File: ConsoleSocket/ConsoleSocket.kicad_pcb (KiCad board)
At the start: 2 copper layers, 112.9 x 12.7 mm, 4 parts, among them J1 Conn_01x05_Male, J3 Conn_02x25_Odd_Even

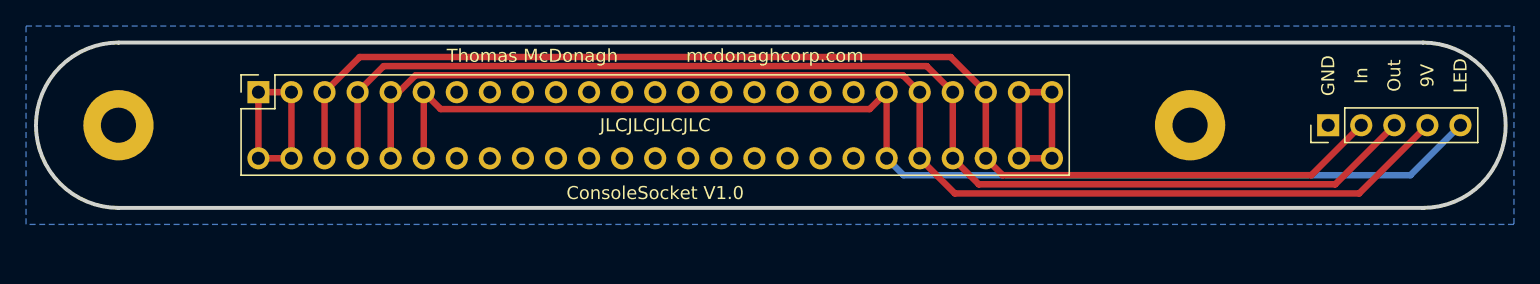
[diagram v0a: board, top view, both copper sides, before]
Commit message: Fixed socket to fit screws and space easier
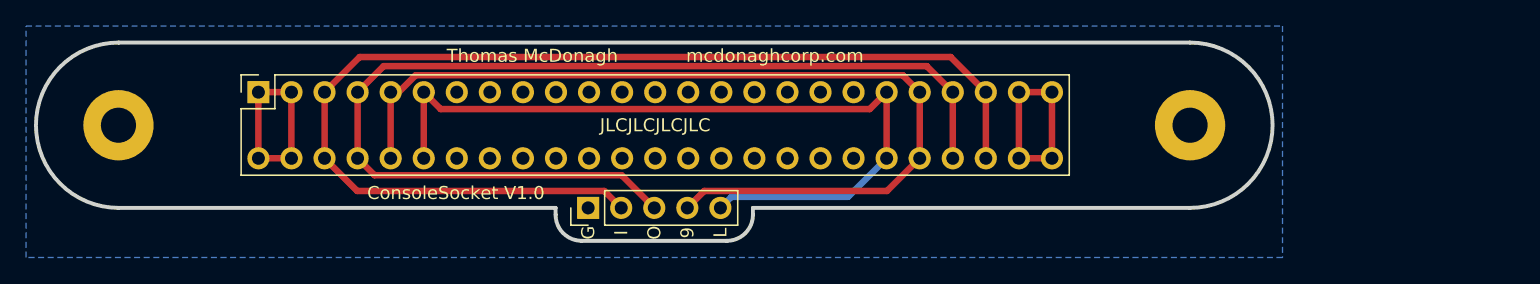
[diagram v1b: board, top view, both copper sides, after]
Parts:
- moved J1 57.2 mm to (132.1, 45.7)
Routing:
- net /LEDPower: track 93.6 -> 61.8 mm
- net +9V: track 94.8 -> 71.9 mm
- net /Output: track 94.2 -> 81.9 mm
- net /Input: track 94.8 -> 88.2 mm
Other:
- board size 112.9 x 12.7 mm -> 95 x 15.2 mm
- board text added: "9"
- board text added: "G"
- board text added: "I"
- board text added: "L"
- board text added: "O"
- board text removed: "9V"
- board text removed: "GND"
- board text removed: "In"
- board text removed: "LED"
- board text removed: "Out"

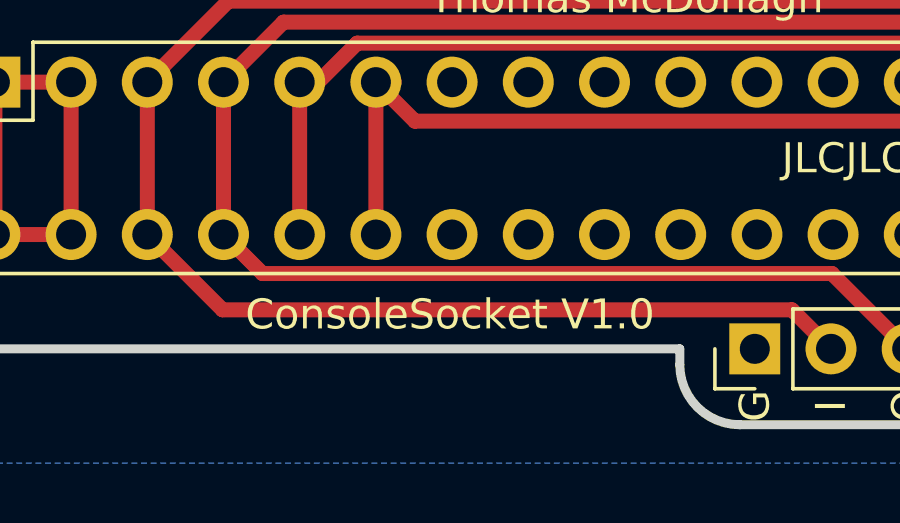
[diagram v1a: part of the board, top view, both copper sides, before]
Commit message: Fixed silkscreen
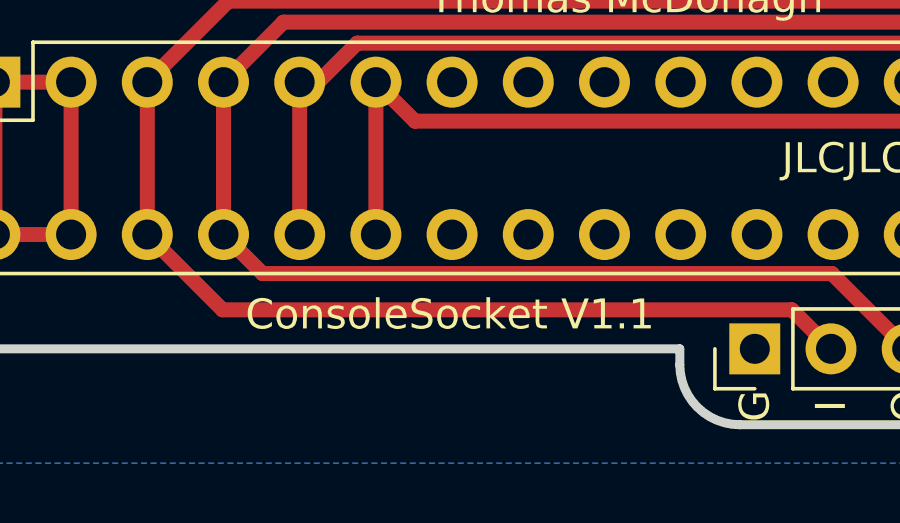
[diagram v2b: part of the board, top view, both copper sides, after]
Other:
- board text added: "ConsoleSocket V1.1"
- board text removed: "ConsoleSocket V1.0"
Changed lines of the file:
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@@
   )
   (setup
-    (last_trace_width 0.5)
+    (last_trace_width 0.25)
     (user_trace_width 0.5)
     (trace_clearance 0.2)
@@
       (effects (font (size 1 1) (thickness 0.15)))
     )
+    (fp_line (start -6.88 62.7) (end -6.88 -1.8) (layer F.CrtYd) (width 0.05))
+    (fp_line (start 1.76 62.7) (end -6.88 62.7) (layer F.CrtYd) (width 0.05))
+    (fp_line (start 1.76 -1.8) (end 1.76 62.7) (layer F.CrtYd) (width 0.05))
+    (fp_line (start -6.88 -1.8) (end 1.76 -1.8) (layer F.CrtYd) (width 0.05))
+    (fp_line (start 0 -1.33) (end 1.33 -1.33) (layer F.SilkS) (width 0.12))
+    (fp_line (start 1.33 -1.33) (end 1.33 0) (layer F.SilkS) (width 0.12))
+    (fp_line (start -1.27 -1.33) (end -1.27 1.27) (layer F.SilkS) (width 0.12))
+    (fp_line (start -1.27 1.27) (end 1.33 1.27) (layer F.SilkS) (width 0.12))
+    (fp_line (start 1.33 1.27) (end 1.33 62.29) (layer F.SilkS) (width 0.12))
+    (fp_line (start -6.38 62.29) (end 1.33 62.29) (layer F.SilkS) (width 0.12))
+    (fp_line (start -6.38 -1.33) (end -6.38 62.29) (layer F.SilkS) (width 0.12))
+    (fp_line (start -6.38 -1.33) (end -1.27 -1.33) (layer F.SilkS) (width 0.12))
+    (fp_line (start -6.35 62.23) (end -6.35 -1.27) (layer F.Fab) (width 0.1))
+    (fp_line (start 1.27 62.23) (end -6.35 62.23) (layer F.Fab) (width 0.1))
+    (fp_line (start 1.27 -0.27) (end 1.27 62.23) (layer F.Fab) (width 0.1))
+    (fp_line (start 0.27 -1.27) (end 1.27 -0.27) (layer F.Fab) (width 0.1))
     (fp_line (start -6.35 -1.27) (end 0.27 -1.27) (layer F.Fab) (width 0.1))
-    (fp_line (start 0.27 -1.27) (end 1.27 -0.27) (layer F.Fab) (width 0.1))
-    (fp_line (start 1.27 -0.27) (end 1.27 62.23) (layer F.Fab) (width 0.1))
-    (fp_line (start 1.27 62.23) (end -6.35 62.23) (layer F.Fab) (width 0.1))
-    (fp_line (start -6.35 62.23) (end -6.35 -1.27) (layer F.Fab) (width 0.1))
-    (fp_line (start -6.38 -1.33) (end -1.27 -1.33) (layer F.SilkS) (width 0.12))
-    (fp_line (start -6.38 -1.33) (end -6.38 62.29) (layer F.SilkS) (width 0.12))
-    (fp_line (start -6.38 62.29) (end 1.33 62.29) (layer F.SilkS) (width 0.12))
-    (fp_line (start 1.33 1.27) (end 1.33 62.29) (layer F.SilkS) (width 0.12))
-    (fp_line (start -1.27 1.27) (end 1.33 1.27) (layer F.SilkS) (width 0.12))
-    (fp_line (start -1.27 -1.33) (end -1.27 1.27) (layer F.SilkS) (width 0.12))
-    (fp_line (start 1.33 -1.33) (end 1.33 0) (layer F.SilkS) (width 0.12))
-    (fp_line (start 0 -1.33) (end 1.33 -1.33) (layer F.SilkS) (width 0.12))
-    (fp_line (start -6.88 -1.8) (end 1.76 -1.8) (layer F.CrtYd) (width 0.05))
-    (fp_line (start 1.76 -1.8) (end 1.76 62.7) (layer F.CrtYd) (width 0.05))
-    (fp_line (start 1.76 62.7) (end -6.88 62.7) (layer F.CrtYd) (width 0.05))
-    (fp_line (start -6.88 62.7) (end -6.88 -1.8) (layer F.CrtYd) (width 0.05))
     (fp_text user %R (at -1.27 30.48 180) (layer F.Fab)
       (effects (font (size 1 1) (thickness 0.15)))
@@
       (effects (font (size 1 1) (thickness 0.15)))
     )
+    (fp_line (start 1.8 -1.8) (end -1.8 -1.8) (layer F.CrtYd) (width 0.05))
+    (fp_line (start 1.8 11.95) (end 1.8 -1.8) (layer F.CrtYd) (width 0.05))
+    (fp_line (start -1.8 11.95) (end 1.8 11.95) (layer F.CrtYd) (width 0.05))
+    (fp_line (start -1.8 -1.8) (end -1.8 11.95) (layer F.CrtYd) (width 0.05))
+    (fp_line (start -1.33 -1.33) (end 0 -1.33) (layer F.SilkS) (width 0.12))
+    (fp_line (start -1.33 0) (end -1.33 -1.33) (layer F.SilkS) (width 0.12))
+    (fp_line (start -1.33 1.27) (end 1.33 1.27) (layer F.SilkS) (width 0.12))
+    (fp_line (start 1.33 1.27) (end 1.33 11.49) (layer F.SilkS) (width 0.12))
+    (fp_line (start -1.33 1.27) (end -1.33 11.49) (layer F.SilkS) (width 0.12))
+    (fp_line (start -1.33 11.49) (end 1.33 11.49) (layer F.SilkS) (width 0.12))
+    (fp_line (start -1.27 -0.635) (end -0.635 -1.27) (layer F.Fab) (width 0.1))
+    (fp_line (start -1.27 11.43) (end -1.27 -0.635) (layer F.Fab) (width 0.1))
+    (fp_line (start 1.27 11.43) (end -1.27 11.43) (layer F.Fab) (width 0.1))
+    (fp_line (start 1.27 -1.27) (end 1.27 11.43) (layer F.Fab) (width 0.1))
     (fp_line (start -0.635 -1.27) (end 1.27 -1.27) (layer F.Fab) (width 0.1))
-    (fp_line (start 1.27 -1.27) (end 1.27 11.43) (layer F.Fab) (width 0.1))
-    (fp_line (start 1.27 11.43) (end -1.27 11.43) (layer F.Fab) (width 0.1))
-    (fp_line (start -1.27 11.43) (end -1.27 -0.635) (layer F.Fab) (width 0.1))
-    (fp_line (start -1.27 -0.635) (end -0.635 -1.27) (layer F.Fab) (width 0.1))
-    (fp_line (start -1.33 11.49) (end 1.33 11.49) (layer F.SilkS) (width 0.12))
-    (fp_line (start -1.33 1.27) (end -1.33 11.49) (layer F.SilkS) (width 0.12))
-    (fp_line (start 1.33 1.27) (end 1.33 11.49) (layer F.SilkS) (width 0.12))
-    (fp_line (start -1.33 1.27) (end 1.33 1.27) (layer F.SilkS) (width 0.12))
-    (fp_line (start -1.33 0) (end -1.33 -1.33) (layer F.SilkS) (width 0.12))
-    (fp_line (start -1.33 -1.33) (end 0 -1.33) (layer F.SilkS) (width 0.12))
-    (fp_line (start -1.8 -1.8) (end -1.8 11.95) (layer F.CrtYd) (width 0.05))
-    (fp_line (start -1.8 11.95) (end 1.8 11.95) (layer F.CrtYd) (width 0.05))
-    (fp_line (start 1.8 11.95) (end 1.8 -1.8) (layer F.CrtYd) (width 0.05))
-    (fp_line (start 1.8 -1.8) (end -1.8 -1.8) (layer F.CrtYd) (width 0.05))
     (fp_text user %R (at 0 5.08) (layer F.Fab)
       (effects (font (size 1 1) (thickness 0.15)))
@@
       (effects (font (size 1 1) (thickness 0.15)))
     )
+    (fp_circle (center 0 0) (end 2.95 0) (layer F.CrtYd) (width 0.05))
     (fp_circle (center 0 0) (end 2.7 0) (layer Cmts.User) (width 0.15))
-    (fp_circle (center 0 0) (end 2.95 0) (layer F.CrtYd) (width 0.05))
     (fp_text user %R (at 0.3 0) (layer F.Fab)
       (effects (font (size 1 1) (thickness 0.15)))
@@
       (effects (font (size 1 1) (thickness 0.15)))
     )
+    (fp_circle (center 0 0) (end 2.7 0) (layer Cmts.User) (width 0.15))
     (fp_circle (center 0 0) (end 2.95 0) (layer F.CrtYd) (width 0.05))
-    (fp_circle (center 0 0) (end 2.7 0) (layer Cmts.User) (width 0.15))
     (fp_text user %R (at 0.3 0) (layer F.Fab)
       (effects (font (size 1 1) (thickness 0.15)))
@@
     (effects (font (size 1 1) (thickness 0.15)) (justify mirror))
   )
-  (gr_text "ConsoleSocket V1.0" (at 121.92 44.577) (layer B.SilkS)
+  (gr_text "ConsoleSocket V1.1" (at 121.92 44.577) (layer B.SilkS)
     (effects (font (size 1 1) (thickness 0.15)) (justify mirror))
   )
-  (gr_text "ConsoleSocket V1.0" (at 121.92 44.577) (layer F.SilkS)
-    (effects (font (size 1 1) (thickness 0.15)))
-  )
+  (gr_text "ConsoleSocket V1.1" (at 121.92 44.577) (layer F.SilkS)
+    (effects (font (size 1 1) (thickness 0.15)))
+  )

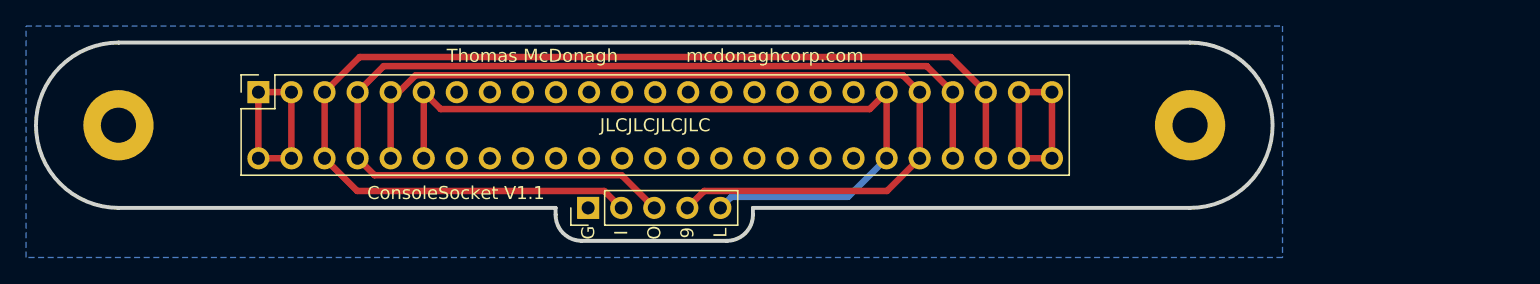
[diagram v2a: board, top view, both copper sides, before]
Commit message: Fixed silkscreen
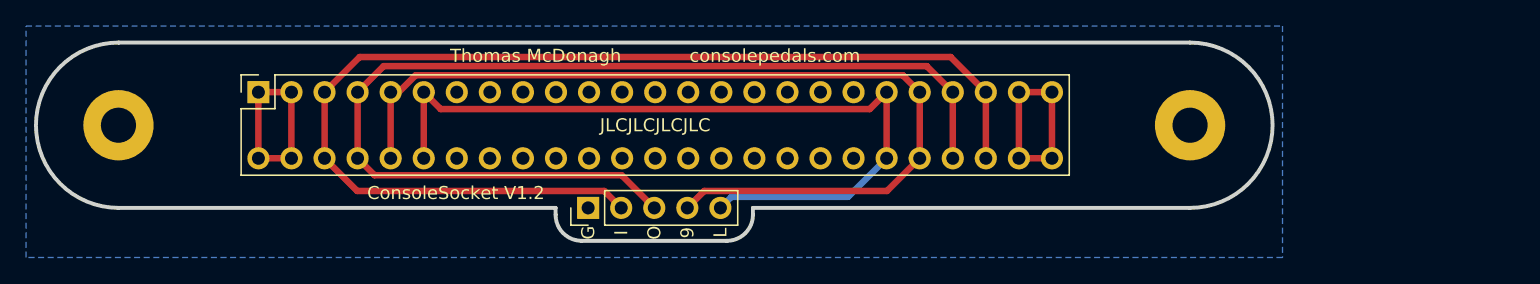
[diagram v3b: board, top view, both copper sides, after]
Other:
- board text added: "ConsoleSocket V1.2"
- board text added: "Thomas McDonagh consolepedals.com"
- board text removed: "ConsoleSocket V1.1"
- board text removed: "Thomas McDonagh mcdonaghcorp.com"
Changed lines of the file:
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@@
   (general
     (thickness 1.6)
-    (drawings 20)
+    (drawings 25)
     (tracks 44)
     (zones 0)
@@
       (effects (font (size 1 1) (thickness 0.15)))
     )
+    (fp_line (start -6.35 -1.27) (end 0.27 -1.27) (layer F.Fab) (width 0.1))
+    (fp_line (start 0.27 -1.27) (end 1.27 -0.27) (layer F.Fab) (width 0.1))
+    (fp_line (start 1.27 -0.27) (end 1.27 62.23) (layer F.Fab) (width 0.1))
+    (fp_line (start 1.27 62.23) (end -6.35 62.23) (layer F.Fab) (width 0.1))
+    (fp_line (start -6.35 62.23) (end -6.35 -1.27) (layer F.Fab) (width 0.1))
+    (fp_line (start -6.38 -1.33) (end -1.27 -1.33) (layer F.SilkS) (width 0.12))
+    (fp_line (start -6.38 -1.33) (end -6.38 62.29) (layer F.SilkS) (width 0.12))
+    (fp_line (start -6.38 62.29) (end 1.33 62.29) (layer F.SilkS) (width 0.12))
+    (fp_line (start 1.33 1.27) (end 1.33 62.29) (layer F.SilkS) (width 0.12))
+    (fp_line (start -1.27 1.27) (end 1.33 1.27) (layer F.SilkS) (width 0.12))
+    (fp_line (start -1.27 -1.33) (end -1.27 1.27) (layer F.SilkS) (width 0.12))
+    (fp_line (start 1.33 -1.33) (end 1.33 0) (layer F.SilkS) (width 0.12))
+    (fp_line (start 0 -1.33) (end 1.33 -1.33) (layer F.SilkS) (width 0.12))
+    (fp_line (start -6.88 -1.8) (end 1.76 -1.8) (layer F.CrtYd) (width 0.05))
+    (fp_line (start 1.76 -1.8) (end 1.76 62.7) (layer F.CrtYd) (width 0.05))
+    (fp_line (start 1.76 62.7) (end -6.88 62.7) (layer F.CrtYd) (width 0.05))
     (fp_line (start -6.88 62.7) (end -6.88 -1.8) (layer F.CrtYd) (width 0.05))
-    (fp_line (start 1.76 62.7) (end -6.88 62.7) (layer F.CrtYd) (width 0.05))
-    (fp_line (start 1.76 -1.8) (end 1.76 62.7) (layer F.CrtYd) (width 0.05))
-    (fp_line (start -6.88 -1.8) (end 1.76 -1.8) (layer F.CrtYd) (width 0.05))
-    (fp_line (start 0 -1.33) (end 1.33 -1.33) (layer F.SilkS) (width 0.12))
-    (fp_line (start 1.33 -1.33) (end 1.33 0) (layer F.SilkS) (width 0.12))
-    (fp_line (start -1.27 -1.33) (end -1.27 1.27) (layer F.SilkS) (width 0.12))
-    (fp_line (start -1.27 1.27) (end 1.33 1.27) (layer F.SilkS) (width 0.12))
-    (fp_line (start 1.33 1.27) (end 1.33 62.29) (layer F.SilkS) (width 0.12))
-    (fp_line (start -6.38 62.29) (end 1.33 62.29) (layer F.SilkS) (width 0.12))
-    (fp_line (start -6.38 -1.33) (end -6.38 62.29) (layer F.SilkS) (width 0.12))
-    (fp_line (start -6.38 -1.33) (end -1.27 -1.33) (layer F.SilkS) (width 0.12))
-    (fp_line (start -6.35 62.23) (end -6.35 -1.27) (layer F.Fab) (width 0.1))
-    (fp_line (start 1.27 62.23) (end -6.35 62.23) (layer F.Fab) (width 0.1))
-    (fp_line (start 1.27 -0.27) (end 1.27 62.23) (layer F.Fab) (width 0.1))
-    (fp_line (start 0.27 -1.27) (end 1.27 -0.27) (layer F.Fab) (width 0.1))
-    (fp_line (start -6.35 -1.27) (end 0.27 -1.27) (layer F.Fab) (width 0.1))
     (fp_text user %R (at -1.27 30.48 180) (layer F.Fab)
       (effects (font (size 1 1) (thickness 0.15)))
@@
       (effects (font (size 1 1) (thickness 0.15)))
     )
+    (fp_line (start -0.635 -1.27) (end 1.27 -1.27) (layer F.Fab) (width 0.1))
+    (fp_line (start 1.27 -1.27) (end 1.27 11.43) (layer F.Fab) (width 0.1))
+    (fp_line (start 1.27 11.43) (end -1.27 11.43) (layer F.Fab) (width 0.1))
+    (fp_line (start -1.27 11.43) (end -1.27 -0.635) (layer F.Fab) (width 0.1))
+    (fp_line (start -1.27 -0.635) (end -0.635 -1.27) (layer F.Fab) (width 0.1))
+    (fp_line (start -1.33 11.49) (end 1.33 11.49) (layer F.SilkS) (width 0.12))
+    (fp_line (start -1.33 1.27) (end -1.33 11.49) (layer F.SilkS) (width 0.12))
+    (fp_line (start 1.33 1.27) (end 1.33 11.49) (layer F.SilkS) (width 0.12))
+    (fp_line (start -1.33 1.27) (end 1.33 1.27) (layer F.SilkS) (width 0.12))
+    (fp_line (start -1.33 0) (end -1.33 -1.33) (layer F.SilkS) (width 0.12))
+    (fp_line (start -1.33 -1.33) (end 0 -1.33) (layer F.SilkS) (width 0.12))
+    (fp_line (start -1.8 -1.8) (end -1.8 11.95) (layer F.CrtYd) (width 0.05))
+    (fp_line (start -1.8 11.95) (end 1.8 11.95) (layer F.CrtYd) (width 0.05))
+    (fp_line (start 1.8 11.95) (end 1.8 -1.8) (layer F.CrtYd) (width 0.05))
     (fp_line (start 1.8 -1.8) (end -1.8 -1.8) (layer F.CrtYd) (width 0.05))
-    (fp_line (start 1.8 11.95) (end 1.8 -1.8) (layer F.CrtYd) (width 0.05))
-    (fp_line (start -1.8 11.95) (end 1.8 11.95) (layer F.CrtYd) (width 0.05))
-    (fp_line (start -1.8 -1.8) (end -1.8 11.95) (layer F.CrtYd) (width 0.05))
-    (fp_line (start -1.33 -1.33) (end 0 -1.33) (layer F.SilkS) (width 0.12))
-    (fp_line (start -1.33 0) (end -1.33 -1.33) (layer F.SilkS) (width 0.12))
-    (fp_line (start -1.33 1.27) (end 1.33 1.27) (layer F.SilkS) (width 0.12))
-    (fp_line (start 1.33 1.27) (end 1.33 11.49) (layer F.SilkS) (width 0.12))
-    (fp_line (start -1.33 1.27) (end -1.33 11.49) (layer F.SilkS) (width 0.12))
-    (fp_line (start -1.33 11.49) (end 1.33 11.49) (layer F.SilkS) (width 0.12))
-    (fp_line (start -1.27 -0.635) (end -0.635 -1.27) (layer F.Fab) (width 0.1))
-    (fp_line (start -1.27 11.43) (end -1.27 -0.635) (layer F.Fab) (width 0.1))
-    (fp_line (start 1.27 11.43) (end -1.27 11.43) (layer F.Fab) (width 0.1))
-    (fp_line (start 1.27 -1.27) (end 1.27 11.43) (layer F.Fab) (width 0.1))
-    (fp_line (start -0.635 -1.27) (end 1.27 -1.27) (layer F.Fab) (width 0.1))
     (fp_text user %R (at 0 5.08) (layer F.Fab)
       (effects (font (size 1 1) (thickness 0.15)))
@@
       (effects (font (size 1 1) (thickness 0.15)))
     )
+    (fp_circle (center 0 0) (end 2.7 0) (layer Cmts.User) (width 0.15))
     (fp_circle (center 0 0) (end 2.95 0) (layer F.CrtYd) (width 0.05))
-    (fp_circle (center 0 0) (end 2.7 0) (layer Cmts.User) (width 0.15))
     (fp_text user %R (at 0.3 0) (layer F.Fab)
       (effects (font (size 1 1) (thickness 0.15)))
@@
       (effects (font (size 1 1) (thickness 0.15)))
     )
+    (fp_circle (center 0 0) (end 2.95 0) (layer F.CrtYd) (width 0.05))
     (fp_circle (center 0 0) (end 2.7 0) (layer Cmts.User) (width 0.15))
-    (fp_circle (center 0 0) (end 2.95 0) (layer F.CrtYd) (width 0.05))
     (fp_text user %R (at 0.3 0) (layer F.Fab)
       (effects (font (size 1 1) (thickness 0.15)))
@@
     (pad 1 thru_hole circle (at 0 0) (size 5.4 5.4) (drill 2.7) (layers *.Cu *.Mask)
       (net 3 GND))
+  )
+  (gr_text "L\n" (at 142.24 47.625 90) (layer F.SilkS)
+    (effects (font (size 1 1) (thickness 0.15)))
+  )
+  (gr_text 9 (at 139.7 47.625 90) (layer F.SilkS)
+    (effects (font (size 1 1) (thickness 0.15)))
+  )
+  (gr_text O (at 137.16 47.625 90) (layer F.SilkS)
+    (effects (font (size 1 1) (thickness 0.15)))
+  )
+  (gr_text I (at 134.62 47.625 90) (layer F.SilkS)
+    (effects (font (size 1 1) (thickness 0.15)))
+  )
+  (gr_text G (at 132.08 47.625 90) (layer F.SilkS)
+    (effects (font (size 1 1) (thickness 0.15)))
   )
   (gr_line (start 144.74 45.72) (end 144.74 46.25) (layer Edge.Cuts) (width 0.3))
@@
   (gr_arc (start 131.58 46.25) (end 129.58 46.25) (angle -90) (layer Edge.Cuts) (width 0.3))
   (gr_arc (start 142.74 46.25) (end 142.74 48.25) (angle -90) (layer Edge.Cuts) (width 0.3))
-  (gr_text "L\n" (at 142.24 47.625 90) (layer F.SilkS)
-    (effects (font (size 1 1) (thickness 0.15)))
-  )
-  (gr_text 9 (at 139.7 47.625 90) (layer F.SilkS)
-    (effects (font (size 1 1) (thickness 0.15)))
-  )
-  (gr_text O (at 137.16 47.625 90) (layer F.SilkS)
-    (effects (font (size 1 1) (thickness 0.15)))
-  )
-  (gr_text I (at 134.62 47.625 90) (layer F.SilkS)
-    (effects (font (size 1 1) (thickness 0.15)))
-  )
-  (gr_text G (at 132.08 47.625 90) (layer F.SilkS)
-    (effects (font (size 1 1) (thickness 0.15)))
-  )
-  (gr_text "Thomas McDonagh            mcdonaghcorp.com" (at 137.23 34.036) (layer B.SilkS)
-    (effects (font (size 1 1) (thickness 0.15)) (justify mirror))
-  )
-  (gr_text "ConsoleSocket V1.1" (at 121.92 44.577) (layer B.SilkS)
-    (effects (font (size 1 1) (thickness 0.15)) (justify mirror))
-  )
-  (gr_text "ConsoleSocket V1.1" (at 121.92 44.577) (layer F.SilkS)
-    (effects (font (size 1 1) (thickness 0.15)))
-  )
-  (gr_text "Thomas McDonagh            mcdonaghcorp.com" (at 137.23 34.036) (layer F.SilkS)
-    (effects (font (size 1 1) (thickness 0.15)))
-  )
+  (gr_text "L\n" (at 142.24 47.625 90) (layer B.SilkS)
+    (effects (font (size 1 1) (thickness 0.15)) (justify mirror))
+  )
+  (gr_text 9 (at 139.7 47.625 90) (layer B.SilkS)
+    (effects (font (size 1 1) (thickness 0.15)) (justify mirror))
+  )
+  (gr_text O (at 137.16 47.625 90) (layer B.SilkS)
+    (effects (font (size 1 1) (thickness 0.15)) (justify mirror))
+  )
+  (gr_text I (at 134.62 47.625 90) (layer B.SilkS)
+    (effects (font (size 1 1) (thickness 0.15)) (justify mirror))
+  )
+  (gr_text G (at 132.08 47.625 90) (layer B.SilkS)
+    (effects (font (size 1 1) (thickness 0.15)) (justify mirror))
+  )
+  (gr_text "Thomas McDonagh            consolepedals.com" (at 137.23 34.036) (layer B.SilkS)
+    (effects (font (size 1 1) (thickness 0.15)) (justify mirror))
+  )
+  (gr_text "ConsoleSocket V1.2" (at 121.92 44.577) (layer B.SilkS)
+    (effects (font (size 1 1) (thickness 0.15)) (justify mirror))
+  )
+  (gr_text "ConsoleSocket V1.2" (at 121.92 44.577) (layer F.SilkS)
+    (effects (font (size 1 1) (thickness 0.15)))
+  )
+  (gr_text "Thomas McDonagh            consolepedals.com" (at 137.23 34.036) (layer F.SilkS)
+    (effects (font (size 1 1) (thickness 0.15)))
+  )
